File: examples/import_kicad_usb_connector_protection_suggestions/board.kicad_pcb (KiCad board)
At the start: 4 parts, among them J1 USB2_CONNECTOR

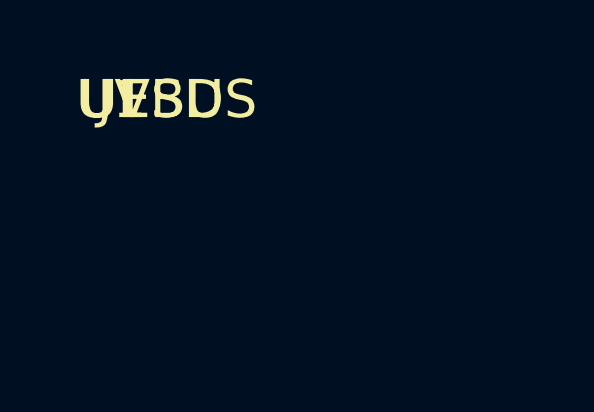
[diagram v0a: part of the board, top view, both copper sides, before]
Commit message: Import KiCad PCB route geometry
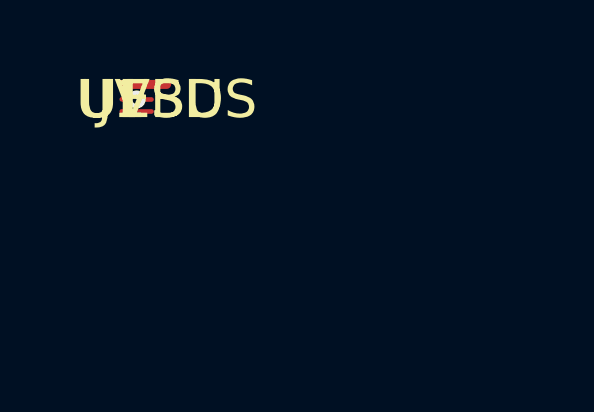
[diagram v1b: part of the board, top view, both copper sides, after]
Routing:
- net USB_VBUS: track 0.00 -> 1.50 mm
- net USB_DP: track 0.00 -> 1.00 mm, vias 0 -> 1
- net USB_DM: track 0.00 -> 1.00 mm
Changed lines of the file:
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@@
   (version 20240108)
   (generator circuitci_fixture)
+  (net 1 "USB_DP")
+  (net 2 "USB_DM")
+  (net 3 "USB_VBUS")
+  (net 4 "GND")
   (footprint "Connector:USB2" (layer "F.Cu")
     (at 0 0 0)
@@
     (at 20 20 0)
     (property "Reference" "H1" (at 0 0 0) (layer "F.SilkS")))
+  (segment (start 0 0) (end 1 0) (width 0.15) (layer "F.Cu") (net 1))
+  (segment (start 0 0.4) (end 1 0.4) (width 0.15) (layer "F.Cu") (net 2))
+  (segment (start 0 -0.5) (end 1.5 -0.5) (width 0.30) (layer "F.Cu") (net 3))
+  (via (at 0.5 0.0) (size 0.60) (drill 0.30) (layers "F.Cu" "B.Cu") (net 1))
 )

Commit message: Import KiCad routing constraints
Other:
- net class USB_HS added: clearance 0.15, trace_width 0.15
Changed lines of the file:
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@@
   (net 3 "USB_VBUS")
   (net 4 "GND")
+  (net_class "USB_HS" "USB high-speed data"
+    (clearance 0.15)
+    (trace_width 0.15)
+    (diff_pair_width 0.15)
+    (diff_pair_gap 0.15)
+    (add_net "USB_DP")
+    (add_net "USB_DM"))
+  (rule "USB data length and skew"
+    (condition "A.hasNetclass('USB_HS')")
+    (constraint length (max 25mm))
+    (constraint skew (max 0.5mm) within_diff_pairs))
   (footprint "Connector:USB2" (layer "F.Cu")
     (at 0 0 0)

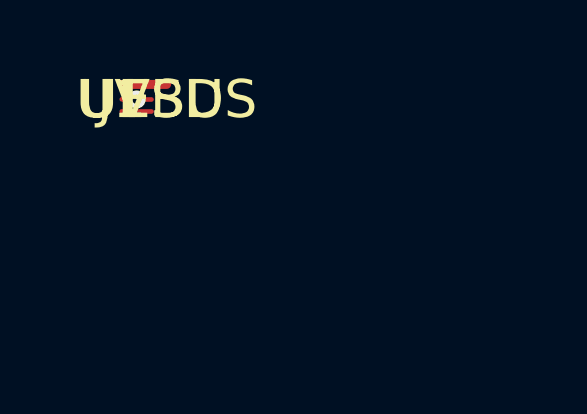
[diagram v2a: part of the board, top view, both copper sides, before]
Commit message: Import KiCad PCB copper zones
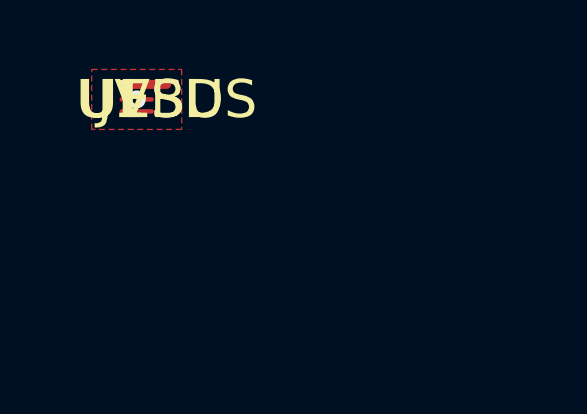
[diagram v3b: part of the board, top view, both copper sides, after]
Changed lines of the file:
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@@
   (segment (start 0 -0.5) (end 1.5 -0.5) (width 0.30) (layer "F.Cu") (net 3))
   (via (at 0.5 0.0) (size 0.60) (drill 0.30) (layers "F.Cu" "B.Cu") (net 1))
+  (zone (net 4) (net_name "GND") (layer "F.Cu")
+    (polygon
+      (pts
+        (xy -1 -1)
+        (xy 2 -1)
+        (xy 2 1)
+        (xy -1 1))))
 )
